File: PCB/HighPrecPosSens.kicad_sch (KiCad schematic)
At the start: 0 parts

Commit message: Valami leiras
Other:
- title: High Precision Linear Position  Sensor -> High Precision Position Sensor
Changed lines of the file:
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@@
   (paper "A3")
   (title_block
-    (title "High Precision Linear Position  Sensor")
-    (date "2022-11-03")
+    (title "High Precision Position Sensor")
+    (date "2023-01-29")
     (rev "1")
     (company "enGYneer")
+    (comment 1 "By Martin Gyurkó")
+    (comment 2 "www.gyurma.de")
+    (comment 3 "www.enGYneer.de")
   )
   (sheet_instances

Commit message: added some parts to it
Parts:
- added C? (x2): 100n, Capacitor_SMD:C_0603_1608Metric, symbol Device:C
- added C? (x2): 22u, Capacitor_SMD:C_0603_1608Metric, symbol Device:C
- added C?: 1u, Capacitor_SMD:C_0603_1608Metric, symbol Device:C
- added U?: S12443, SensorLibrary:s12443, symbol Sensor CMOS:S12443
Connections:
- new net: C?.1, C?.1, U?.1 (Vdd)
- new net: C?.1, U?.13 (Vcp)
- new net: C?.1, C?.1, U?.7 (Vdd)
- new net GND: C?.2, C?.2, C?.2, C?.2, C?.2, U?.3 (Vss), U?.6 (Vss)

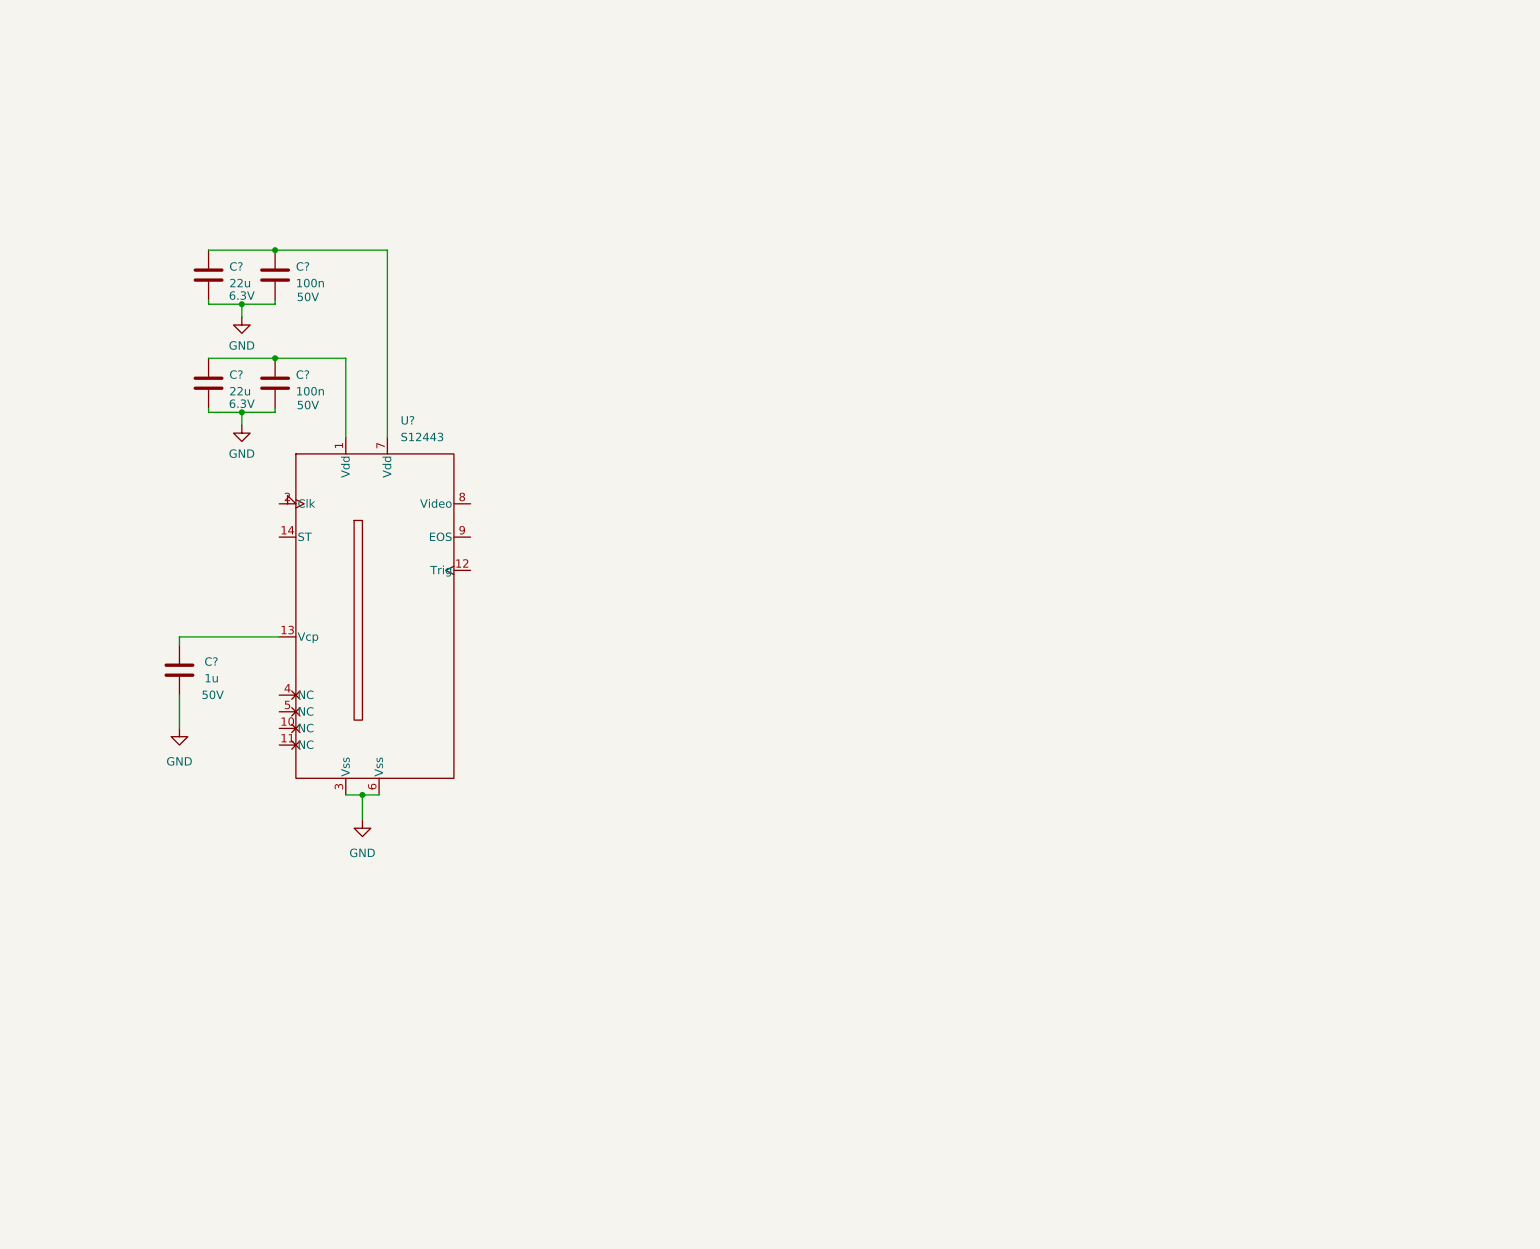
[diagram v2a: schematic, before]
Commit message: Added 2 bit ADC
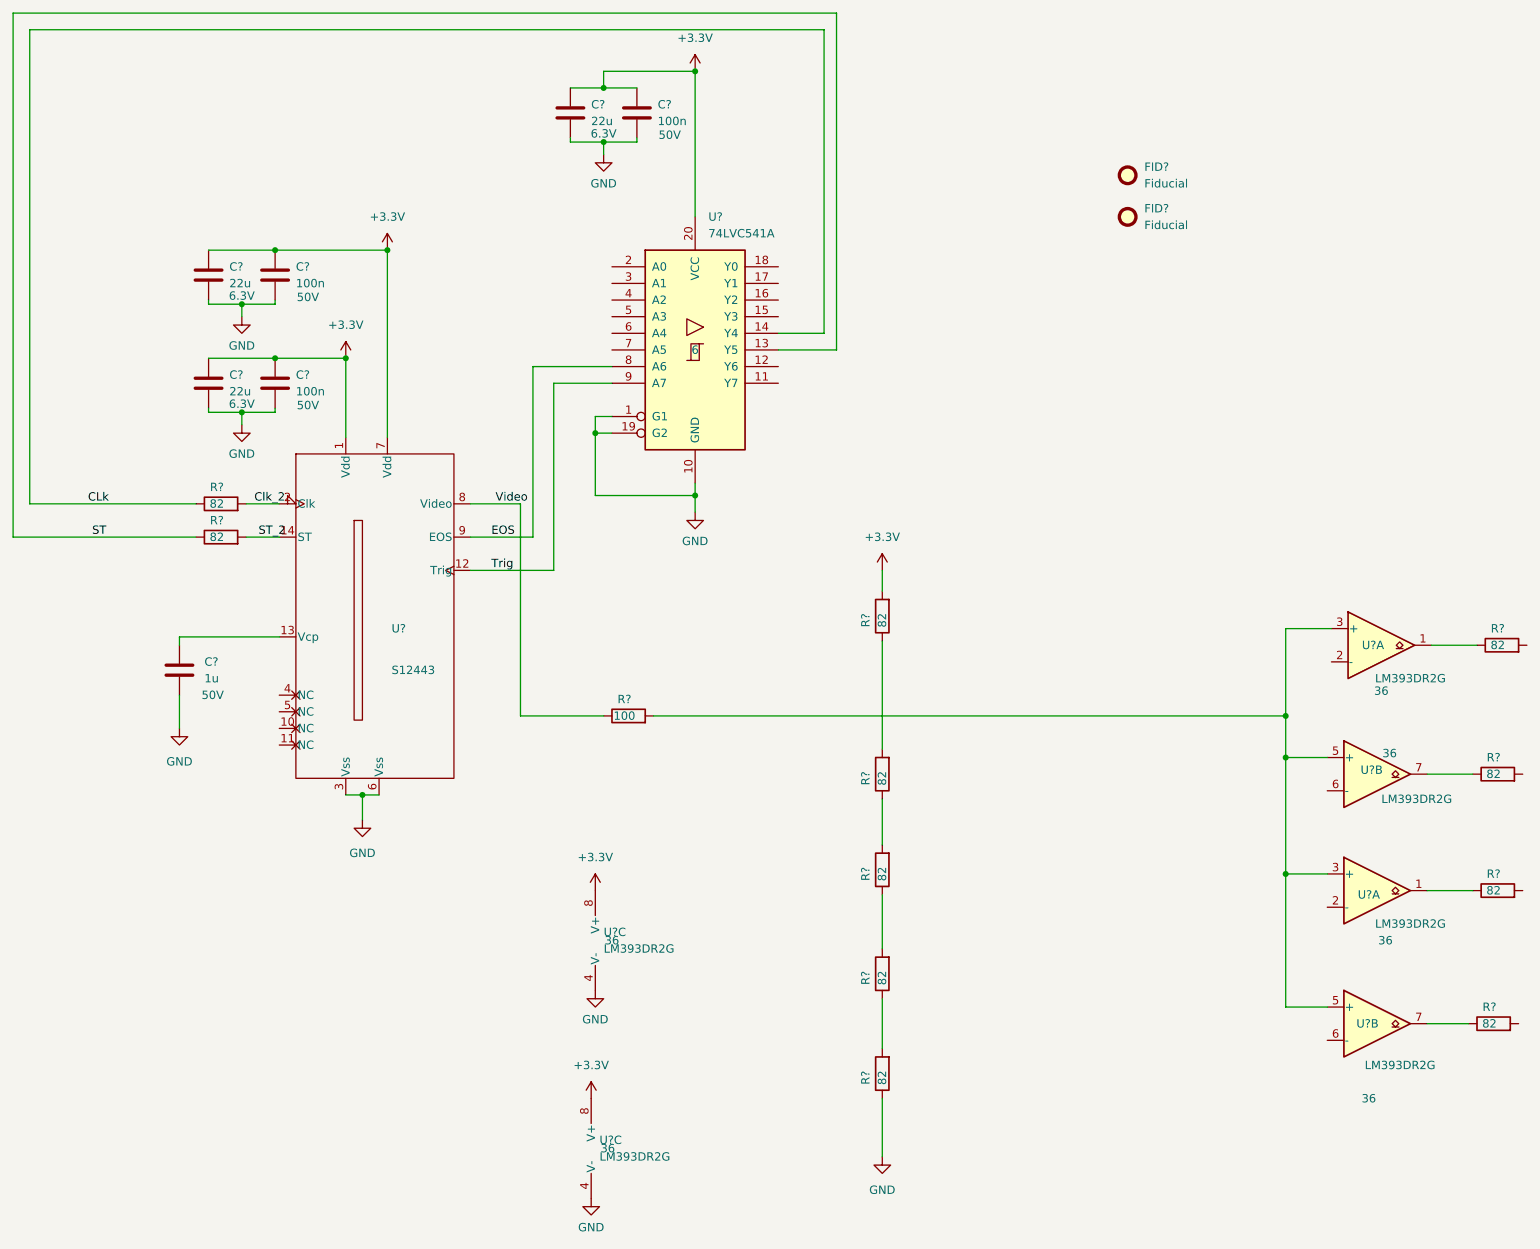
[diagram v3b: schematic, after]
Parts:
- added C?: 100n, Capacitor_SMD:C_0603_1608Metric, symbol Device:C
- added C?: 22u, Capacitor_SMD:C_0603_1608Metric, symbol Device:C
- added FID? (x2): Fiducial, Fiducial:Fiducial_1mm_Mask2mm, symbol Mechanical:Fiducial
- added R? (x11): 82, Resistor_SMD:R_0603_1608Metric, symbol Device:R
- added R?: 100, Resistor_SMD:R_0603_1608Metric, symbol Device:R
- added U? (x6): LM393DR2G, Package_SO:SOIC-8_3.9x4.9mm_P1.27mm, symbol Comparator:LM393
- added U?: 74LVC541A, Package_SO:TSSOP-20_4.4x6.5mm_P0.65mm, symbol 74xx:74HCT541
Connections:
- net GND: now also C?.2, C?.2, R?.1, U?.1 (G1), U?.10 (GND), U?.19 (G2), U?.4 (V-), U?.4 (V-)
- net +3.3V: now reaches C?.1, C?.1, U?.1 (Vdd)
- net +3.3V: now also C?.1, C?.1, U?.7 (Vdd), C?.1, C?.1, R?.2, U?.20 (VCC), U?.8 (V+), U?.8 (V+)
- net Trig: now reaches U?.12 (Trig)
- net Trig: now also U?.9 (A7)
- net ST_2: now reaches U?.14 (ST)
- net ST_2: now also R?.2
- net Clk_2: now reaches U?.2 (Clk)
- net Clk_2: now also R?.2
- net Video: now reaches U?.8 (Video)
- net Video: now also R?.1
- net EOS: now reaches U?.9 (EOS)
- net EOS: now also U?.8 (A6)
- new net: R?.2, U?.3 (+), U?.3 (+), U?.5 (+), U?.5 (+)
- new net: R?.1, U?.7 (x2)
- new net: R?.1, U?.1 (x2)
- new net: R?.1, R?.2 (x4)
- new net CLk: R?.1, U?.14 (Y4)
- new net ST: R?.1, U?.13 (Y5)

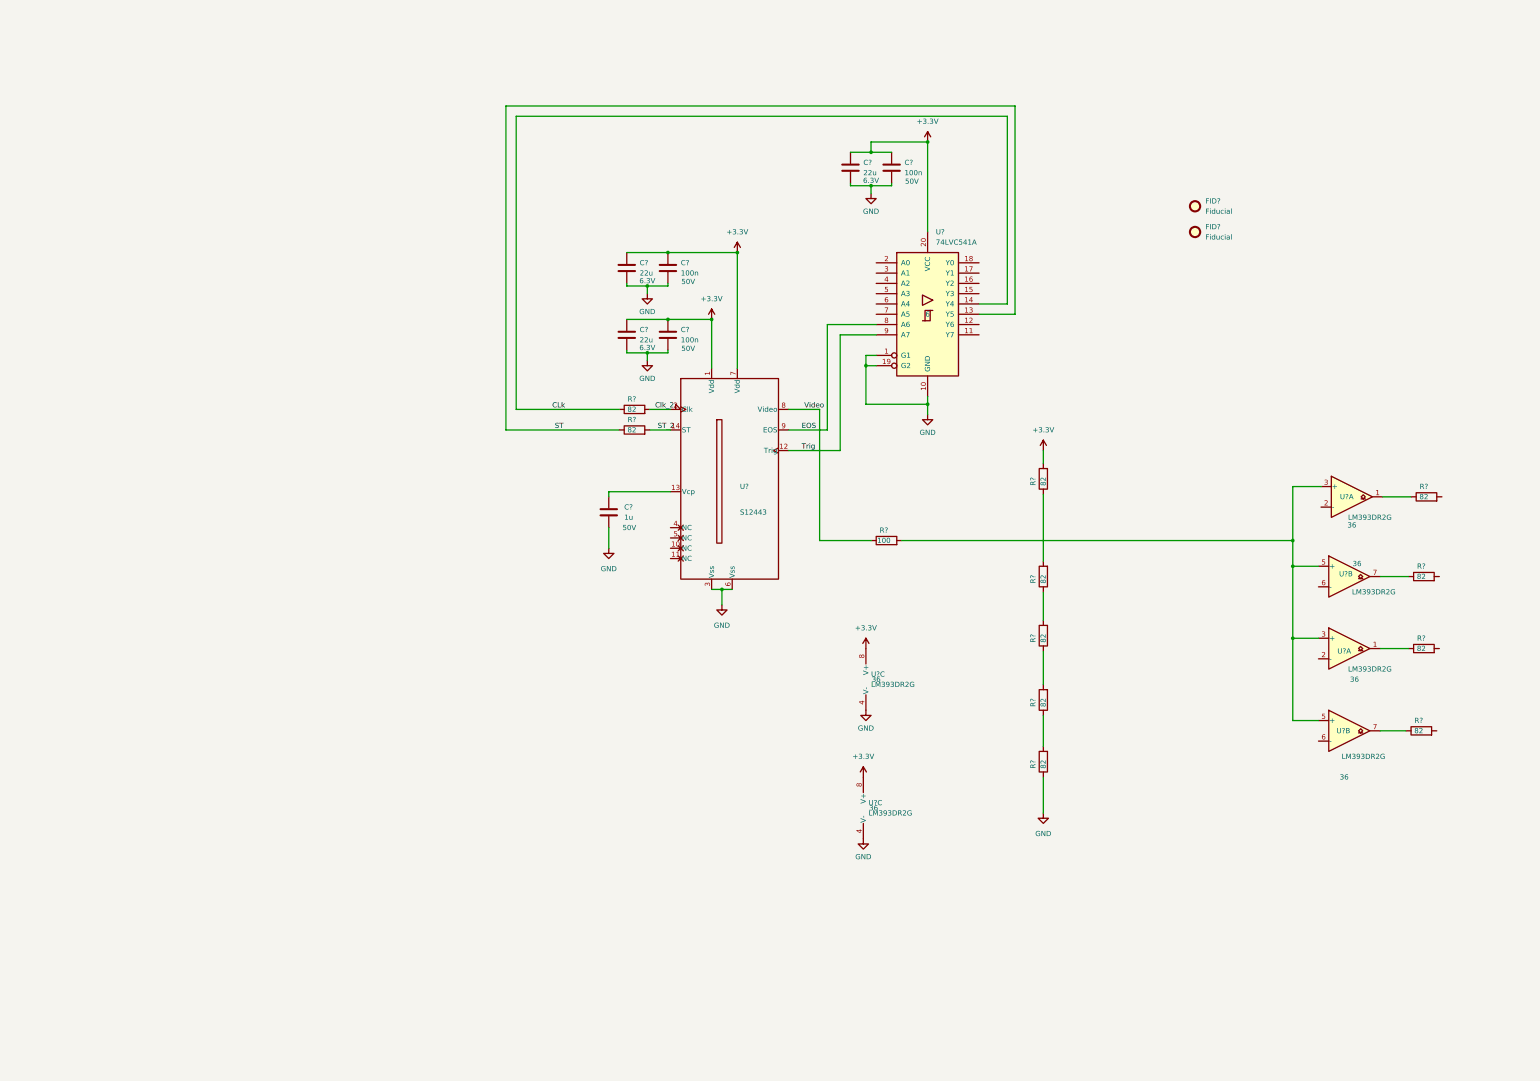
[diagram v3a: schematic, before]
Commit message: Added 2 bit ADC ladder and comparators
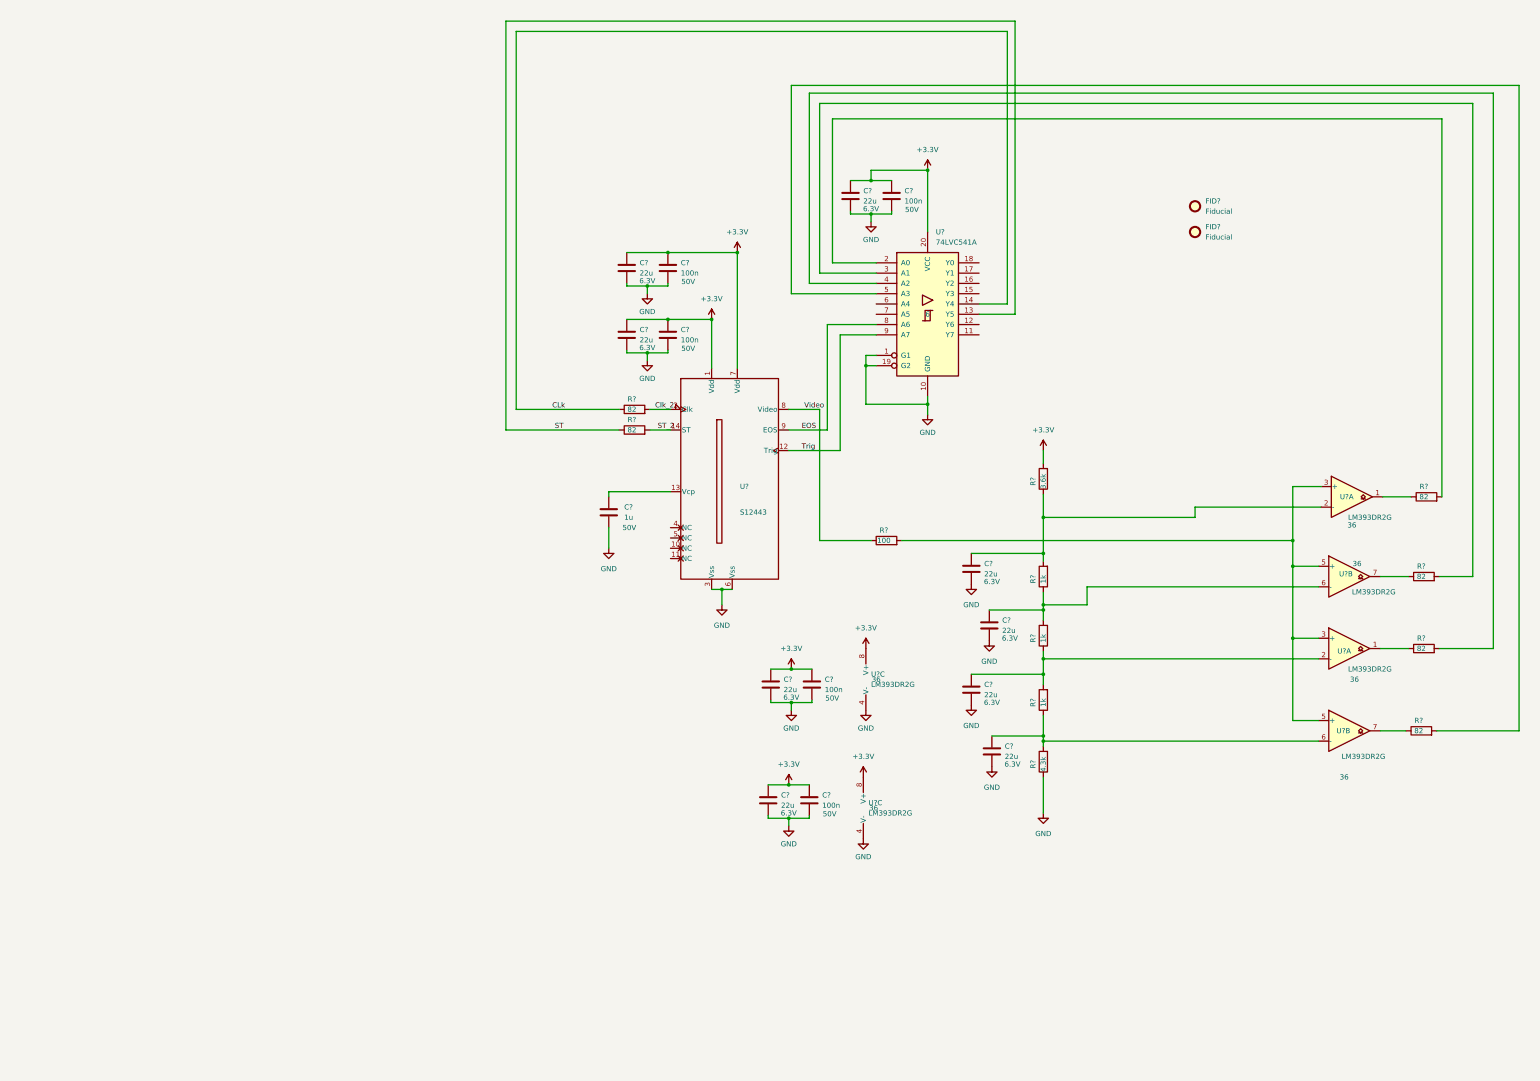
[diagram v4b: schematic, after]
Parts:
- removed R? (x2): 82, Resistor_SMD:R_0603_1608Metric, symbol Device:R
- added C? (x6): 22u, Capacitor_SMD:C_0603_1608Metric, symbol Device:C
- added C? (x2): 100n, Capacitor_SMD:C_0603_1608Metric, symbol Device:C
- added R? (x2): 1k, Resistor_SMD:R_0603_1608Metric, symbol Device:R
- R?: value 82 -> 3.6k; ManufacturerPartNum 0603WAF820JT5E -> 0603WAF3601T5E; SourcingPartNum C23255 -> C22980
- R?: value 82 -> 4.3k; ManufacturerPartNum 0603WAF820JT5E -> 0603WAF4301T5E; SourcingPartNum C23255 -> C23159
- R?: value 82 -> 1k; ManufacturerPartNum 0603WAF820JT5E -> 0603WAF1001T5E; SourcingPartNum C23255 -> C21190
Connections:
- net +3.3V: now also C?.1, C?.1, C?.1, C?.1
- net GND: now also C?.2, C?.2, C?.2, C?.2, C?.2, C?.2, C?.2, C?.2
- net at U?.6 (-): now also R?.1, C?.1, R?.2
- net at U?.2 (-): now also R?.1, R?.2, C?.1
- net at U?.2 (-): now also C?.1, R?.1, R?.2
- net at R?.2: now also U?.5 (A3)
- net at R?.2: now also U?.6 (-), C?.1, R?.1
- net at R?.2: now also U?.2 (A0)
- net at R?.2: now also U?.4 (A2)
- net at U?.3 (A1): now also R?.2
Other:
- moved on the sheet: C?
